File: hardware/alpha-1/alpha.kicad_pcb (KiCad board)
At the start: 2 copper layers, 65 x 56 mm, 82 parts, among them J1 POWER, J2 SERIAL, P1 SWITCH_1, P2 SWITCH_2, P3 SWITCH_3, P4 SWITCH_4, P5 SWITCH_5, P6 SWITCH_6, P7 INPUTS, P8 RASPBERRY_PI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

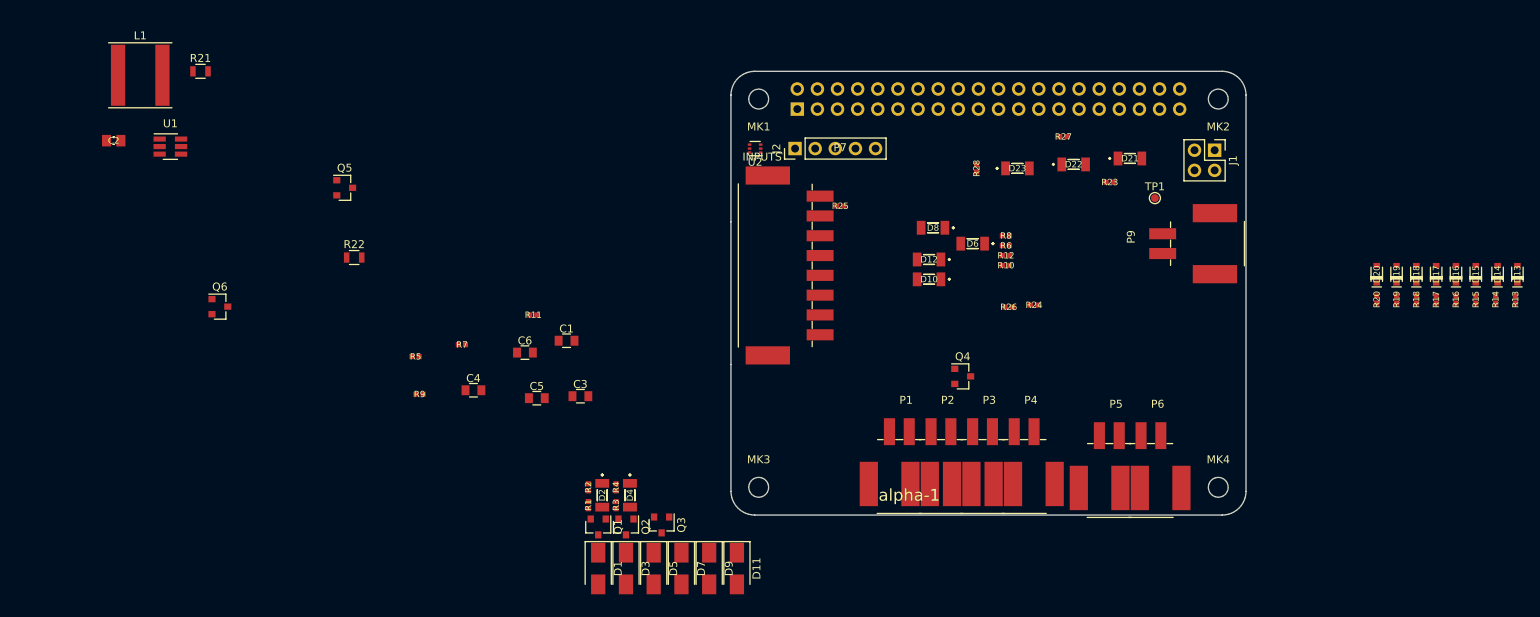
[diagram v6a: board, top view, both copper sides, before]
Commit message: o Changing connectors from Phoenix PTSM to Harting har-flexicon. o Combing all outputs into a single output terminal to save some space. Will make up for it with slik print.
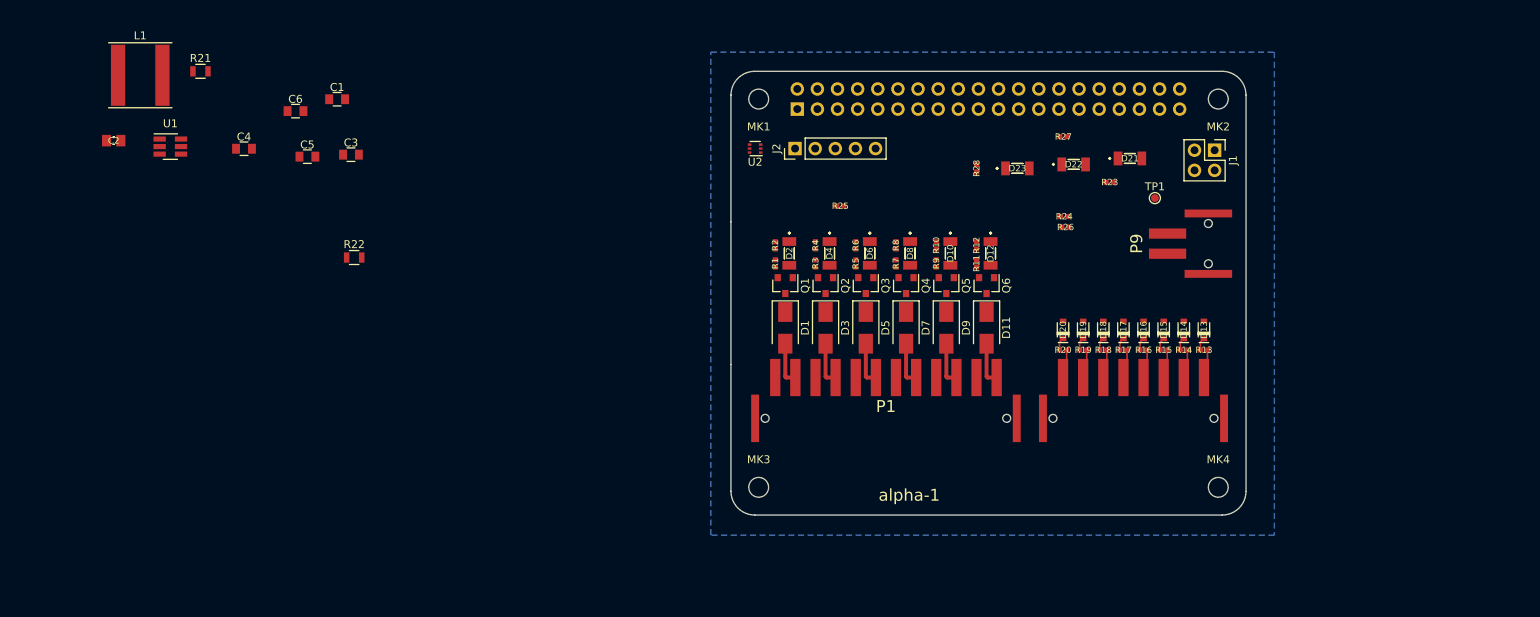
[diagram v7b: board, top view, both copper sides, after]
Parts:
- removed P2: SWITCH_2, Bitraf:PhoenixContact_PTSM_0,5_2-2,5-H_SMD
- removed P3: SWITCH_3, Bitraf:PhoenixContact_PTSM_0,5_2-2,5-H_SMD
- removed P4: SWITCH_4, Bitraf:PhoenixContact_PTSM_0,5_2-2,5-H_SMD
- removed P5: SWITCH_5, Bitraf:PhoenixContact_PTSM_0,5_2-2,5-H_SMD
- removed P6: SWITCH_6, Bitraf:PhoenixContact_PTSM_0,5_2-2,5-H_SMD
- P1: value SWITCH_1 -> OUTPUTS; footprint Bitraf:PhoenixContact_PTSM_0,5_2-2,5-H_SMD -> Bitraf:har-flexicon_2,54_TSPH-12_T56_BK
- P7: footprint Bitraf:PhoenixContact_PTSM_0,5_8-2,5-H_SMD -> Bitraf:har-flexicon_2,54_TSPH-08_T56_BK
- P9: footprint Bitraf:PhoenixContact_PTSM_0,5_2-2,5-H_SMD -> Bitraf:har-flexicon_2,54_TSPH-02_T56_BK
- moved Q6 96.8 mm to (232.3, 121.0), turned to 270 degrees
- moved Q5 76.9 mm to (227.2, 121.0), turned to 270 degrees
- moved R9 67.3 mm to (225.9, 118.2), turned to 90 degrees
- moved R5 56.8 mm to (215.7, 118.2), turned to 270 degrees
- moved R11 56.3 mm to (231.0, 118.2), turned to 270 degrees
- moved R7 55.7 mm to (220.8, 118.2), turned to 270 degrees
- moved P7 48.3 mm to (250.8, 137.0), turned to 180 degrees
- moved D11 43.8 mm to (232.3, 126.4)
- moved D9 42.6 mm to (227.2, 126.4)
- moved C1 42.0 mm to (150.3, 97.5)
- moved C3 42.0 mm to (152.0, 104.5)
- moved C4 42.0 mm to (138.5, 103.8)
- moved C5 42.0 mm to (146.5, 104.8)
- moved C6 42.0 mm to (145.0, 99.0)
- moved D7 41.5 mm to (222.1, 126.4)
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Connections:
- D1 pad 2: Net-(D1-Pad2) -> /SWITCH_1_OUT
- D11 pad 2: Net-(D11-Pad2) -> /SWITCH_6_OUT
- D3 pad 2: Net-(D3-Pad2) -> /SWITCH_2_OUT
- D5 pad 2: Net-(D5-Pad2) -> /SWITCH_3_OUT
- D7 pad 2: Net-(D7-Pad2) -> /SWITCH_4_OUT
- D9 pad 2: Net-(D9-Pad2) -> /SWITCH_5_OUT
- P1 pad 1: Vin -> /SWITCH_6_OUT
- P1 pad 2: Net-(D1-Pad2) -> Vin
- Q1 pad 3: Net-(D1-Pad2) -> /SWITCH_1_OUT
- Q2 pad 3: Net-(D3-Pad2) -> /SWITCH_2_OUT
- Q3 pad 3: Net-(D5-Pad2) -> /SWITCH_3_OUT
- Q4 pad 3: Net-(D7-Pad2) -> /SWITCH_4_OUT
- Q5 pad 3: Net-(D9-Pad2) -> /SWITCH_5_OUT
- Q6 pad 3: Net-(D11-Pad2) -> /SWITCH_6_OUT
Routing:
- net /SWITCH_5_OUT: track 0.00 -> 5.47 mm
- net /SWITCH_3_OUT: track 0.00 -> 5.47 mm
- net /SWITCH_2_OUT: track 0.00 -> 5.47 mm
- net /SWITCH_6_OUT: track 0.00 -> 5.47 mm
- net /SWITCH_4_OUT: track 0.00 -> 5.47 mm
- net /SWITCH_1_OUT: track 0.00 -> 5.47 mm
- net Net-(P7-Pad2): track 0.00 -> 3.66 mm
- net Net-(P7-Pad8): track 0.00 -> 3.66 mm
- net Net-(P7-Pad7): track 0.00 -> 3.66 mm
- net Net-(P7-Pad4): track 0.00 -> 3.66 mm
- net Net-(P7-Pad6): track 0.00 -> 3.66 mm
- net Net-(P7-Pad5): track 0.00 -> 3.66 mm
- net Net-(P7-Pad3): track 0.00 -> 3.66 mm
- net Net-(P7-Pad1): track 0.00 -> 3.66 mm
- net /INPUT_6: track 0.00 -> 1.61 mm
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- added copper zone on B.Cu, net GND

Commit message: o Routing most of the board.
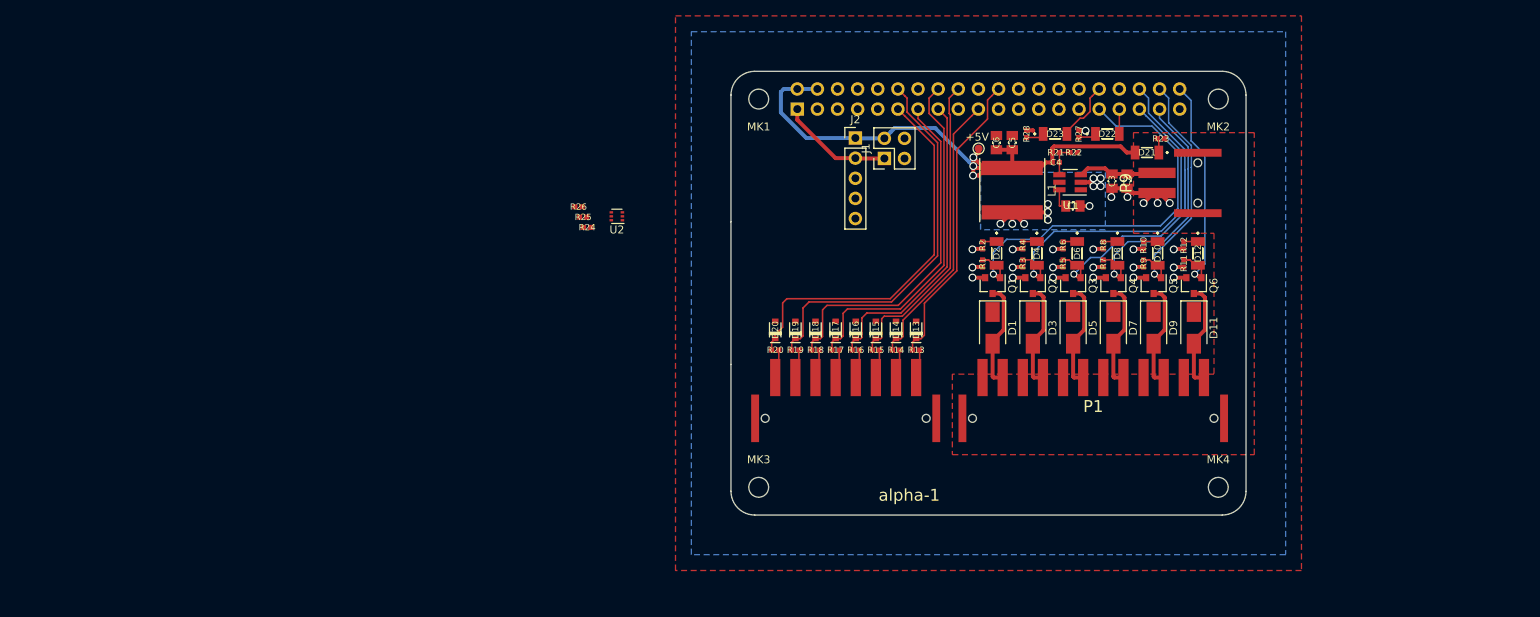
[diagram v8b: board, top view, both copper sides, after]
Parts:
- C1, C3, C5, C6: footprint Capacitors_SMD:C_0805 -> IPC7351-Nominal:CAPC2012X70
- C4: footprint Capacitors_SMD:C_0805 -> IPC7351-Nominal:CAPC1005X55
- D21: value LED -> POWER
- D22: value LED -> STATUS_1
- D23: value LED -> STATUS_2
- R21, R22: footprint Resistors_SMD:R_0805 -> IPC7351-Nominal:RESC1005X38
- moved C2 128.0 mm to (250.0, 107.9), turned to 270 degrees
- moved U1 113.6 mm to (242.8, 108.0), turned to 180 degrees
- moved L1 111.0 mm to (235.5, 109.0), turned to 270 degrees
- moved R21 108.4 mm to (241.0, 104.2)
- moved C4 102.5 mm to (241.0, 105.5)
- moved C3 96.1 mm to (248.1, 107.9), turned to 270 degrees
- moved C1 93.8 mm to (243.2, 111.0)
- moved R22 91.8 mm to (243.2, 104.2)
- moved C5 89.0 mm to (235.5, 103.0), turned to 90 degrees
- moved C6 88.5 mm to (233.5, 103.0), turned to 90 degrees
- moved R26 61.5 mm to (180.8, 111.1)
- moved R24 60.2 mm to (181.8, 113.7)
- moved J1 41.7 mm to (219.4, 105.0), turned to 90 degrees
- moved D13 36.3 mm to (223.4, 126.6)
- moved D15 36.3 mm to (218.3, 126.6)
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- renumbered P8 to U3
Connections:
- net /GPIO11(SPI0_SCK) renamed Net-(U3-Pad23)
- net /GPIO12(PWM0) renamed /STATUS_LED_1
- net /GPIO13(PWM1) renamed /STATUS_LED_2
- net /GPIO14(TXD0) renamed /SERIAL_TX
- net /GPIO15(RXD0) renamed /SERIAL_RX
- net /GPIO2(SDA1) renamed /TMP102_SDA
- net /GPIO3(SCL1) renamed /TMP102_SCL
- net /GPIO5 renamed Net-(U3-Pad29)
- net /GPIO7(SPI1_CE_N) renamed Net-(U3-Pad26)
- net /GPIO8(SPI0_CE_N) renamed Net-(U3-Pad24)
- net /GPIO9(SPI0_MISO) renamed Net-(U3-Pad21)
- net /ID_SC renamed Net-(U3-Pad28)
- net /ID_SD renamed Net-(U3-Pad27)
- net Net-(C1-Pad1) renamed /BOOT
- net Net-(C1-Pad2) renamed /SW
- net Net-(C4-Pad2) renamed /FB
- C2 pad 1: +12V -> Vin
- C3 pad 1: +12V -> Vin
- P9 pad 1: +12V -> Vin
- R24 pad 1: /GPIO16 -> /TMP102_PWR
- R25 pad 1: /GPIO16 -> /TMP102_PWR
- R26 pad 1: /GPIO16 -> /TMP102_PWR
- U1 pad 3: +12V -> Vin
- U2 pad 5: /GPIO16 -> /TMP102_PWR
- U3 pad 11: /GPIO17(GEN0) -> /INPUT_8
- U3 pad 12: /GPIO18(GEN1)(PWM0) -> /INPUT_7
- U3 pad 13: /GPIO27(GEN2) -> /INPUT_6
- U3 pad 15: /GPIO22(GEN3) -> /INPUT_4
- U3 pad 16: /GPIO23(GEN4) -> /INPUT_5
- U3 pad 18: /GPIO24(GEN5) -> /INPUT_3
- U3 pad 19: /GPIO10(SPI0_MOSI) -> /INPUT_2
- U3 pad 22: /GPIO25(GEN6) -> /INPUT_1
- U3 pad 31: /GPIO6 -> /SWITCH_1
- U3 pad 35: /GPIO19(SPI1_MISO) -> /SWITCH_2
- U3 pad 36: /GPIO16 -> /SWITCH_3
- U3 pad 37: /GPIO26 -> /SWITCH_4
- U3 pad 38: /GPIO20(SPI1_MOSI) -> /SWITCH_5
- U3 pad 40: /GPIO21(SPI1_SCK) -> /SWITCH_6
- U3 pad 7: /GPIO4(GCLK) -> /TMP102_PWR
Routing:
- net +5V: track 0.00 -> 77.4 mm, vias 0 -> 3
- net /SWITCH_1: track 0.00 -> 52.5 mm, vias 0 -> 1
- net /INPUT_7: track 1.61 -> 49.1 mm
- net /INPUT_8: track 1.61 -> 48.4 mm
- net /SWITCH_2: track 0.00 -> 43.5 mm, vias 0 -> 1
- net /INPUT_5: track 1.61 -> 44.3 mm
- net /INPUT_6: track 1.61 -> 43.9 mm
- net GND: track 0.00 -> 40.7 mm, vias 0 -> 24
- net /SWITCH_3: track 0.00 -> 40.0 mm, vias 0 -> 1
- net /INPUT_3: track 1.61 -> 39.3 mm
- net /INPUT_4: track 1.61 -> 38.7 mm
- net /INPUT_1: track 1.61 -> 37.8 mm
- net /SWITCH_4: track 0.00 -> 33.7 mm, vias 0 -> 1
- net /INPUT_2: track 1.61 -> 35.3 mm
- net /SWITCH_5: track 0.00 -> 31.8 mm, vias 0 -> 1
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- added copper zone on B.Cu, net /SW
- added copper zone on F.Cu, net GND
- added copper zone on F.Cu, net Vin
